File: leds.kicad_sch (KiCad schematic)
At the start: 23 parts, among them Q1 BSS138

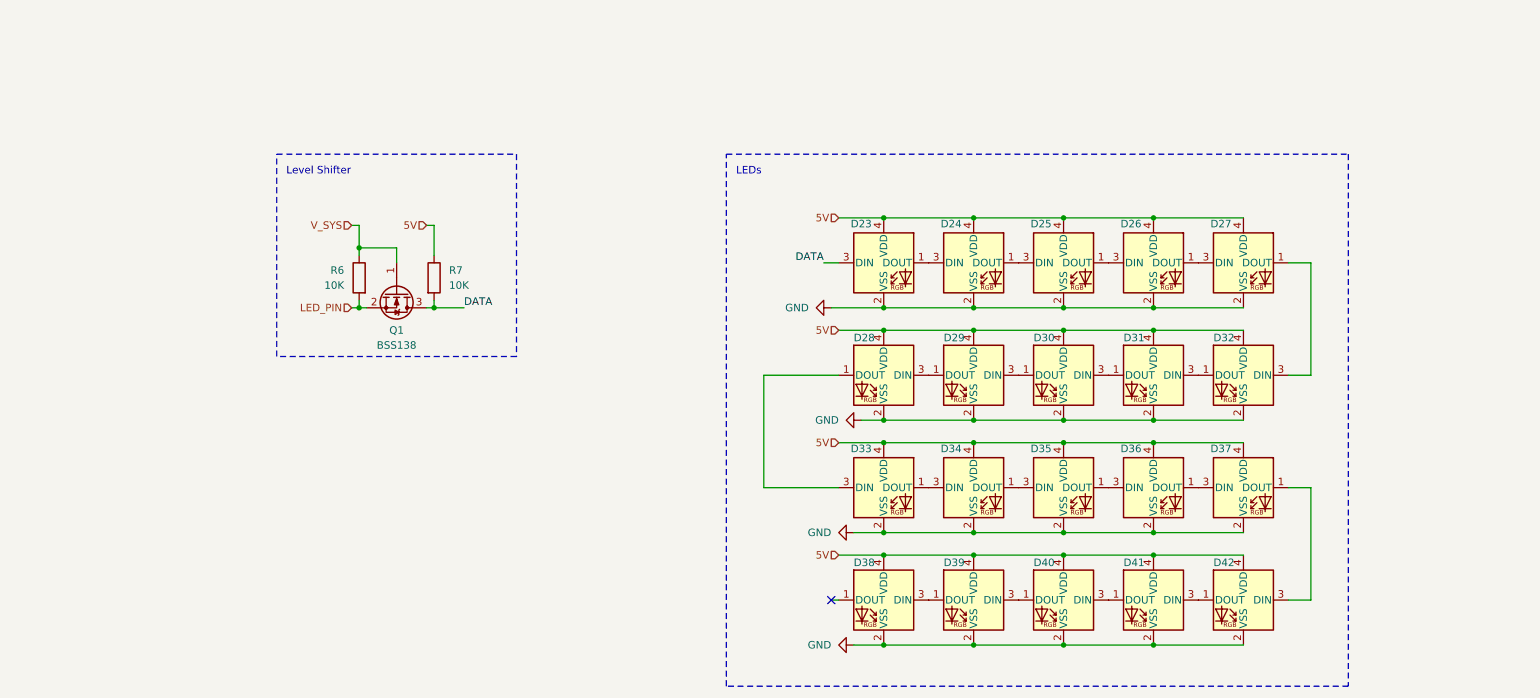
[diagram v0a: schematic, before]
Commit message: switched oout led footprint
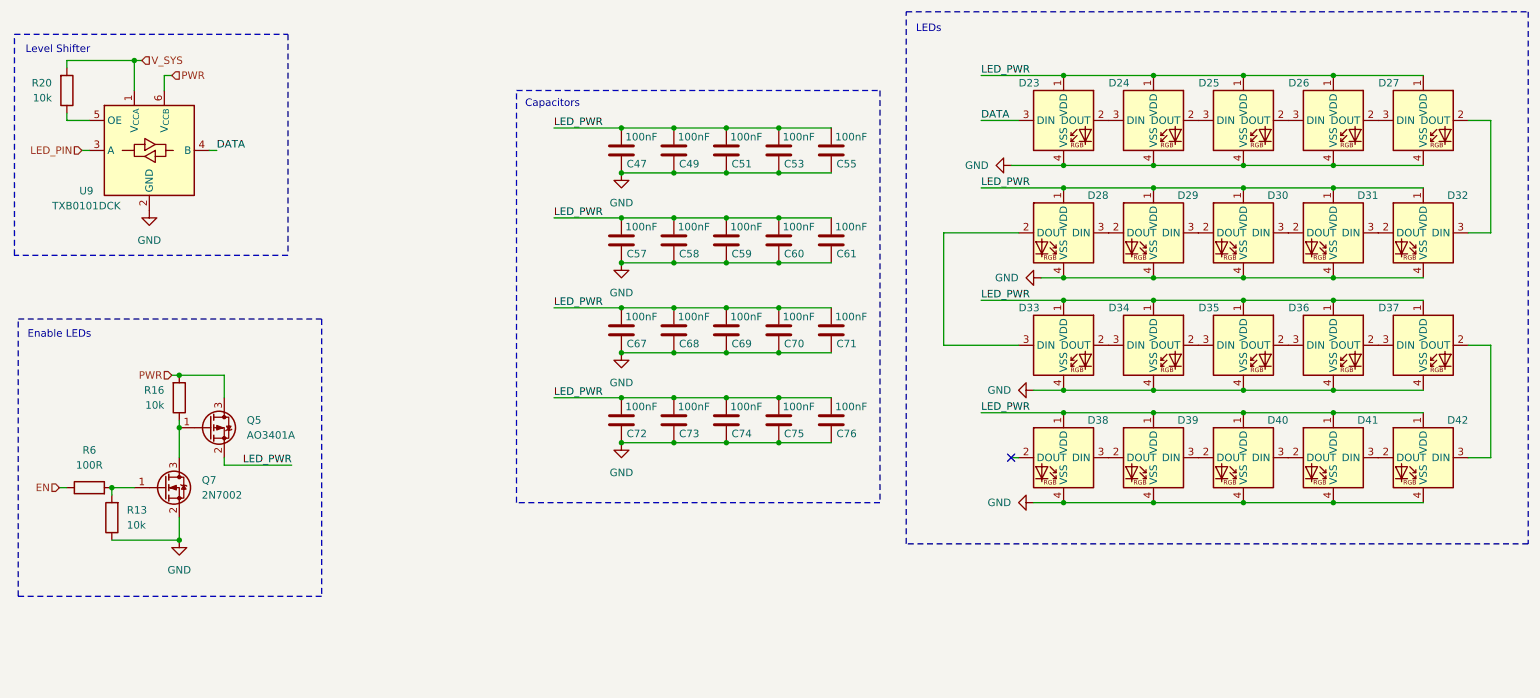
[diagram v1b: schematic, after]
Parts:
- removed D23, D24, D25, D26, D27, D28, D29, D30, D31, D32, D33, D34, D35, D36, D37, D38, D39, D40, D41, D42: SK6812MINI, Keebio_Parts:SK6812-MINI-E, symbol LED:SK6812MINI
- removed Q1: BSS138, Package_TO_SOT_SMD:SOT-23, symbol Transistor_FET:BSS138
- removed R7: 10K, Resistor_SMD:R_0402_1005Metric, symbol Device:R
- added C47, C49, C51, C53, C55, C57, C58, C59, C60, C61, C67, C68, C69, C70, C71, C72, C73, C74, C75, C76: 100nF, Capacitor_SMD:C_0402_1005Metric, symbol Device:C
- added D23, D24, D25, D26, D27, D28, D29, D30, D31, D32, D33, D34, D35, D36, D37, D38, D39, D40, D41, D42: SK6812MINI-E, PCM_marbastlib-various:LED_6028R, symbol PCM_marbastlib-various:SK6812MINI-E
- added Q5: AO3401A, Package_TO_SOT_SMD:SOT-23, symbol Transistor_FET:AO3401A
- added Q7: 2N7002, Package_TO_SOT_SMD:SOT-23, symbol Transistor_FET:2N7002
- added R13, R16, R20: 10k, Resistor_SMD:R_0402_1005Metric, symbol Device:R
- added U9: TXB0101DCK, Package_TO_SOT_SMD:SOT-363_SC-70-6, symbol Logic_LevelTranslator:TXB0101DCK
- R6: value 10K -> 100R
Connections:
- net DATA: now also D23.3 (DIN), U9.4 (B)
- net GND: now also C47.1, C49.1, C51.1, C53.1, C55.1, C57.1, C58.1, C59.1, C60.1, C61.1, C67.1, C68.1, C69.1, C70.1, C71.1, C72.1, C73.1, C74.1, C75.1, C76.1, D23.4 (VSS), D24.4 (VSS), D25.4 (VSS), D26.4 (VSS), D27.4 (VSS), D28.4 (VSS), D29.4 (VSS), D30.4 (VSS), D31.4 (VSS), D32.4 (VSS), D33.4 (VSS), D34.4 (VSS), D35.4 (VSS), D36.4 (VSS), D37.4 (VSS), D38.4 (VSS), D39.4 (VSS), D40.4 (VSS), D41.4 (VSS), D42.4 (VSS), Q7.2 (S), R13.1, U9.2 (GND)
- net LED_PIN: now also U9.3 (A); no longer R6.2
- net V_SYS: now also R20.2, U9.1 (V_{CCA}); no longer R6.1
- new net: D38.3 (DIN), D39.2 (DOUT)
- new net: D39.3 (DIN), D40.2 (DOUT)
- new net: D31.3 (DIN), D32.2 (DOUT)
- new net: D27.2 (DOUT), D32.3 (DIN)
- new net: D34.2 (DOUT), D35.3 (DIN)
- new net: D33.2 (DOUT), D34.3 (DIN)
- new net: D36.2 (DOUT), D37.3 (DIN)
- new net: D35.2 (DOUT), D36.3 (DIN)
- new net: Q5.1 (G), Q7.3 (D), R16.1
- new net: R20.1, U9.5 (OE)
- new net: Q7.1 (G), R13.2, R6.2
- new net: D23.2 (DOUT), D24.3 (DIN)
- new net: D28.3 (DIN), D29.2 (DOUT)
- new net: D29.3 (DIN), D30.2 (DOUT)
- new net: D28.2 (DOUT), D33.3 (DIN)
- new net: D41.3 (DIN), D42.2 (DOUT)
- new net: D37.2 (DOUT), D42.3 (DIN)
- new net: D24.2 (DOUT), D25.3 (DIN)
- new net: D30.3 (DIN), D31.2 (DOUT)
- new net: D26.2 (DOUT), D27.3 (DIN)
- new net: D25.2 (DOUT), D26.3 (DIN)
- new net: D40.3 (DIN), D41.2 (DOUT)
- new net EN: R6.1
- new net LED_PWR: C47.2, C49.2, C51.2, C53.2, C55.2, C57.2, C58.2, C59.2, C60.2, C61.2, C67.2, C68.2, C69.2, C70.2, C71.2, C72.2, C73.2, C74.2, C75.2, C76.2, D23.1 (VDD), D24.1 (VDD), D25.1 (VDD), D26.1 (VDD), D27.1 (VDD), D28.1 (VDD), D29.1 (VDD), D30.1 (VDD), D31.1 (VDD), D32.1 (VDD), D33.1 (VDD), D34.1 (VDD), D35.1 (VDD), D36.1 (VDD), D37.1 (VDD), D38.1 (VDD), D39.1 (VDD), D40.1 (VDD), D41.1 (VDD), D42.1 (VDD), Q5.2 (S)
- new net PWR: Q5.3 (D), R16.2, U9.6 (V_{CCB})
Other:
- note added: "Capacitors"
- note added: "Enable LEDs"
